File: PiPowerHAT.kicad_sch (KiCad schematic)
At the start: 34 parts, among them J8 2444

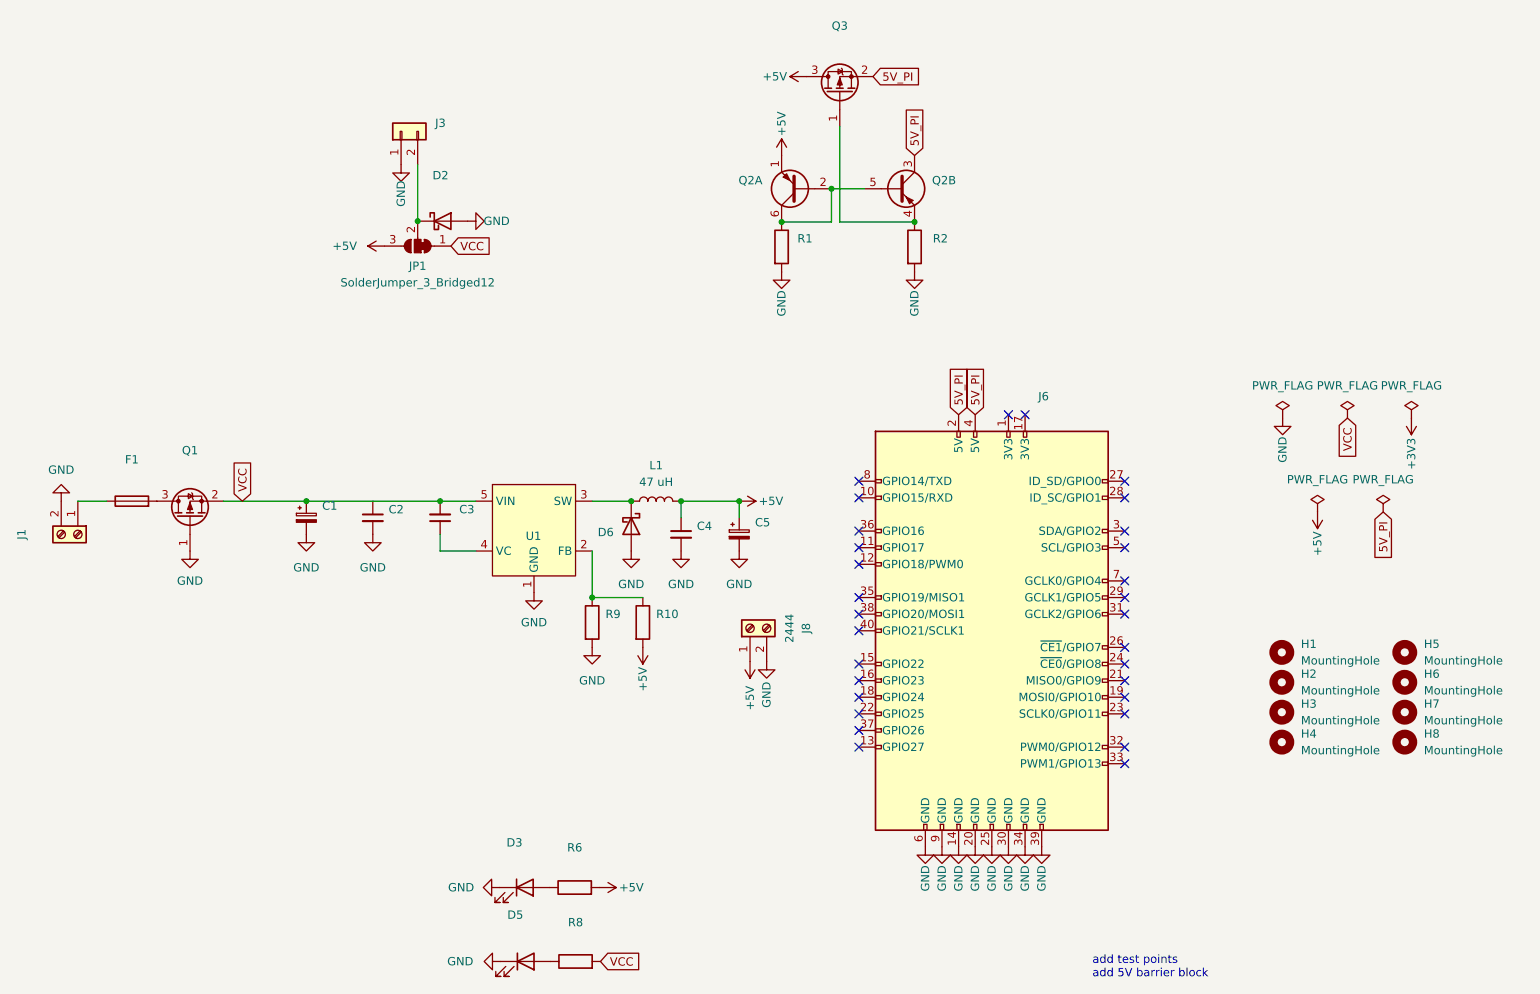
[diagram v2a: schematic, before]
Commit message: BOM Updates
Mounting holes and other items not sent to automated manufacture excluded from BOM
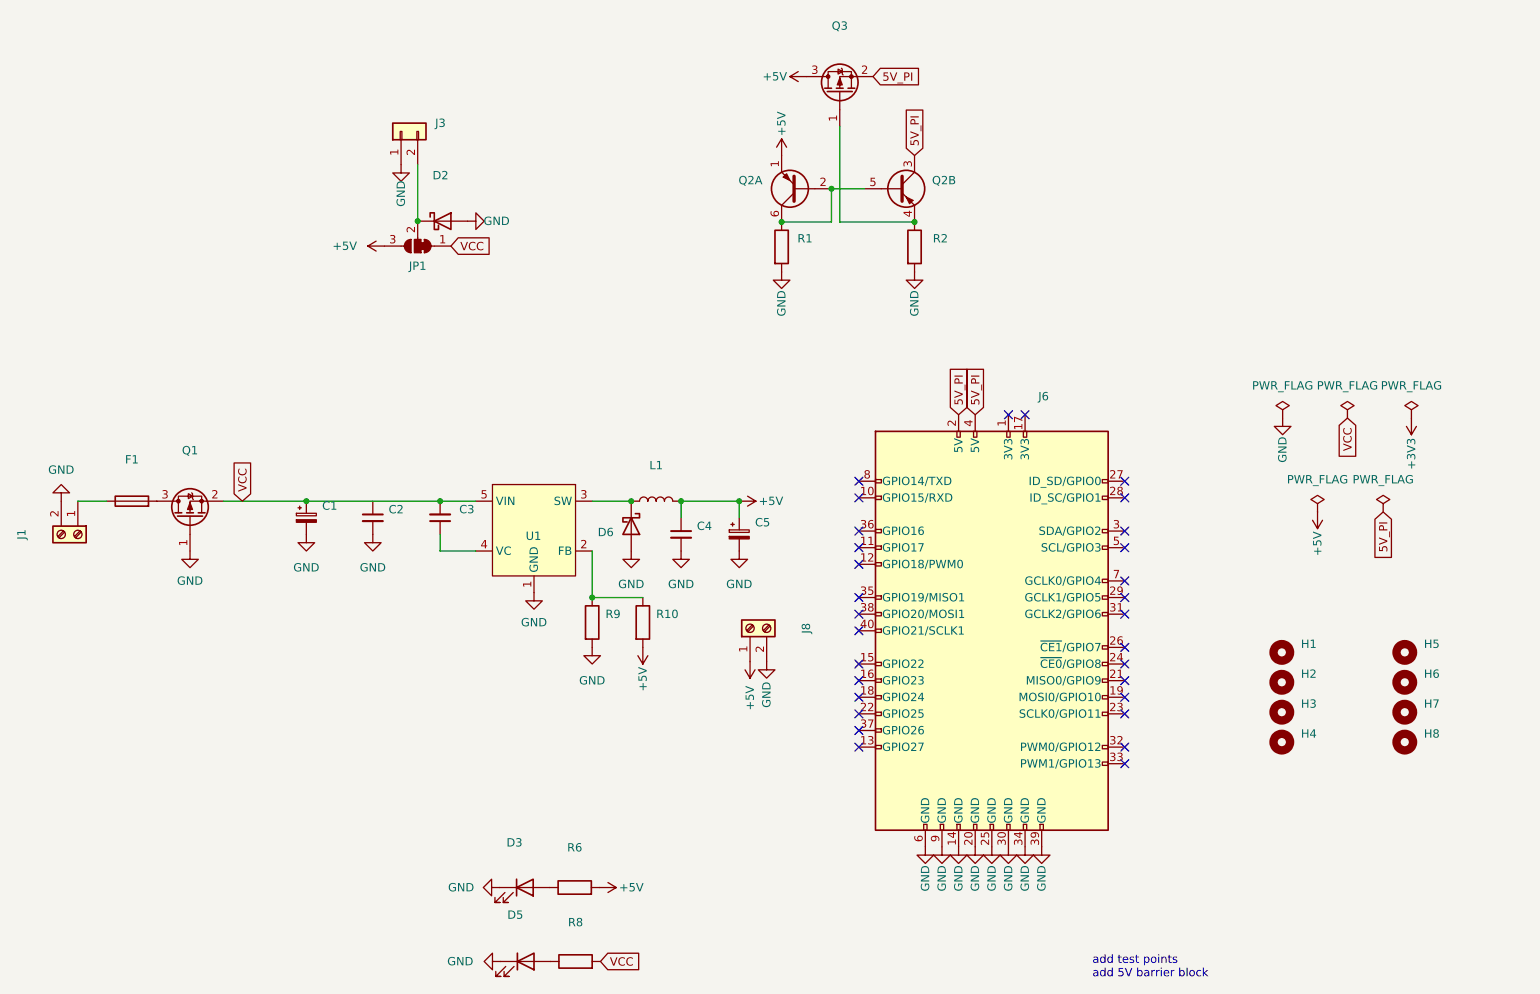
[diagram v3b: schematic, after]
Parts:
- H1, H2, H3, H4: value MountingHole -> (none); footprint MountingHole:MountingHole_2.7mm_M2.5_DIN965_Pad -> (none); now left out of the parts list
- H5, H6, H7, H8: value MountingHole -> (none); footprint MountingHole:MountingHole_3.5mm -> (none); now left out of the parts list
- J1, J3, J6: now left out of the parts list
- J8: value 2444 -> (none); footprint TerminalBlock_4Ucon:TerminalBlock_4Ucon_1x02_P3.50mm_Horizontal -> (none); now left out of the parts list
- JP1: value SolderJumper_3_Bridged12 -> (none); footprint Jumper:SolderJumper-3_P1.3mm_Bridged2Bar12_RoundedPad1.0x1.5mm -> (none); now left out of the parts list
- L1: value 47 uH -> (none); footprint Inductor_SMD:L_12x12mm_H6mm -> (none); JLC C497913 -> (none); LCSC (none) -> C497913
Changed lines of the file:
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@@
   )
   (symbol (lib_id "Mechanical:MountingHole") (at 206.629 132.461 0) (unit 1)
-    (in_bom yes) (on_board yes) (fields_autoplaced)
+    (in_bom no) (on_board yes) (fields_autoplaced)
     (property "Reference" "H4" (id 0) (at 209.55 131.1909 0)
       (effects (font (size 1.27 1.27)) (justify left))
     )
-    (property "Value" "MountingHole" (id 1) (at 209.55 133.7309 0)
-      (effects (font (size 1.27 1.27)) (justify left))
-    )
-    (property "Footprint" "MountingHole:MountingHole_2.7mm_M2.5_DIN965_Pad" (id 2) (at 206.629 132.461 0)
+    (property "Value" "" (id 1) (at 209.55 133.7309 0)
+      (effects (font (size 1.27 1.27)) (justify left))
+    )
+    (property "Footprint" "" (id 2) (at 206.629 132.461 0)
       (effects (font (size 1.27 1.27)) hide)
     )
@@
   )
   (symbol (lib_id "Connector_Generic:Conn_01x02") (at 72.009 39.116 90) (unit 1)
-    (in_bom yes) (on_board yes) (fields_autoplaced)
+    (in_bom no) (on_board yes) (fields_autoplaced)
     (property "Reference" "J3" (id 0) (at 77.216 37.8459 90)
       (effects (font (size 1.27 1.27)) (justify right))
@@
   )
   (symbol (lib_id "Connector:Screw_Terminal_01x02") (at 22.606 100.711 270) (unit 1)
-    (in_bom yes) (on_board yes)
+    (in_bom no) (on_board yes)
     (property "Reference" "J1" (id 0) (at 14.0208 100.711 0))
     (property "Value" "" (id 1) (at 16.5608 100.711 0))
@@
   )
   (symbol (lib_id "Mechanical:MountingHole") (at 206.629 127.889 0) (unit 1)
-    (in_bom yes) (on_board yes) (fields_autoplaced)
+    (in_bom no) (on_board yes) (fields_autoplaced)
     (property "Reference" "H3" (id 0) (at 209.55 126.6189 0)
       (effects (font (size 1.27 1.27)) (justify left))
     )
-    (property "Value" "MountingHole" (id 1) (at 209.55 129.1589 0)
-      (effects (font (size 1.27 1.27)) (justify left))
-    )
-    (property "Footprint" "MountingHole:MountingHole_2.7mm_M2.5_DIN965_Pad" (id 2) (at 206.629 127.889 0)
+    (property "Value" "" (id 1) (at 209.55 129.1589 0)
+      (effects (font (size 1.27 1.27)) (justify left))
+    )
+    (property "Footprint" "" (id 2) (at 206.629 127.889 0)
       (effects (font (size 1.27 1.27)) hide)
     )
@@
   )
   (symbol (lib_id "Mechanical:MountingHole") (at 206.629 123.317 0) (unit 1)
-    (in_bom yes) (on_board yes) (fields_autoplaced)
+    (in_bom no) (on_board yes) (fields_autoplaced)
     (property "Reference" "H2" (id 0) (at 209.55 122.0469 0)
       (effects (font (size 1.27 1.27)) (justify left))
     )
-    (property "Value" "MountingHole" (id 1) (at 209.55 124.5869 0)
-      (effects (font (size 1.27 1.27)) (justify left))
-    )
-    (property "Footprint" "MountingHole:MountingHole_2.7mm_M2.5_DIN965_Pad" (id 2) (at 206.629 123.317 0)
+    (property "Value" "" (id 1) (at 209.55 124.5869 0)
+      (effects (font (size 1.27 1.27)) (justify left))
+    )
+    (property "Footprint" "" (id 2) (at 206.629 123.317 0)
       (effects (font (size 1.27 1.27)) hide)
     )
@@
   )
   (symbol (lib_id "Mechanical:MountingHole") (at 225.425 127.889 0) (unit 1)
-    (in_bom yes) (on_board yes) (fields_autoplaced)
+    (in_bom no) (on_board yes) (fields_autoplaced)
     (property "Reference" "H7" (id 0) (at 228.346 126.6189 0)
       (effects (font (size 1.27 1.27)) (justify left))
     )
-    (property "Value" "MountingHole" (id 1) (at 228.346 129.1589 0)
-      (effects (font (size 1.27 1.27)) (justify left))
-    )
-    (property "Footprint" "MountingHole:MountingHole_3.5mm" (id 2) (at 225.425 127.889 0)
+    (property "Value" "" (id 1) (at 228.346 129.1589 0)
+      (effects (font (size 1.27 1.27)) (justify left))
+    )
+    (property "Footprint" "" (id 2) (at 225.425 127.889 0)
       (effects (font (size 1.27 1.27)) hide)
     )
@@
   )
   (symbol (lib_id "Mechanical:MountingHole") (at 225.425 118.745 0) (unit 1)
-    (in_bom yes) (on_board yes) (fields_autoplaced)
+    (in_bom no) (on_board yes) (fields_autoplaced)
     (property "Reference" "H5" (id 0) (at 228.346 117.4749 0)
       (effects (font (size 1.27 1.27)) (justify left))
     )
-    (property "Value" "MountingHole" (id 1) (at 228.346 120.0149 0)
-      (effects (font (size 1.27 1.27)) (justify left))
-    )
-    (property "Footprint" "MountingHole:MountingHole_3.5mm" (id 2) (at 225.425 118.745 0)
+    (property "Value" "" (id 1) (at 228.346 120.0149 0)
+      (effects (font (size 1.27 1.27)) (justify left))
+    )
+    (property "Footprint" "" (id 2) (at 225.425 118.745 0)
       (effects (font (size 1.27 1.27)) hide)
     )
@@
   )
   (symbol (lib_id "Jumper:SolderJumper_3_Bridged12") (at 74.549 56.642 180) (unit 1)
-    (in_bom yes) (on_board yes) (fields_autoplaced)
+    (in_bom no) (on_board yes) (fields_autoplaced)
     (property "Reference" "JP1" (id 0) (at 74.549 59.69 0))
-    (property "Value" "SolderJumper_3_Bridged12" (id 1) (at 74.549 62.23 0))
-    (property "Footprint" "Jumper:SolderJumper-3_P1.3mm_Bridged2Bar12_RoundedPad1.0x1.5mm" (id 2) (at 74.549 56.642 0)
+    (property "Value" "" (id 1) (at 74.549 62.23 0))
+    (property "Footprint" "" (id 2) (at 74.549 56.642 0)
       (effects (font (size 1.27 1.27)) hide)
     )
@@
   )
   (symbol (lib_id "Mechanical:MountingHole") (at 225.425 132.461 0) (unit 1)
-    (in_bom yes) (on_board yes) (fields_autoplaced)
+    (in_bom no) (on_board yes) (fields_autoplaced)
     (property "Reference" "H8" (id 0) (at 228.346 131.1909 0)
       (effects (font (size 1.27 1.27)) (justify left))
     )
-    (property "Value" "MountingHole" (id 1) (at 228.346 133.7309 0)
-      (effects (font (size 1.27 1.27)) (justify left))
-    )
-    (property "Footprint" "MountingHole:MountingHole_3.5mm" (id 2) (at 225.425 132.461 0)
+    (property "Value" "" (id 1) (at 228.346 133.7309 0)
+      (effects (font (size 1.27 1.27)) (justify left))
+    )
+    (property "Footprint" "" (id 2) (at 225.425 132.461 0)
       (effects (font (size 1.27 1.27)) hide)
     )
@@
   )
   (symbol (lib_id "Connector:Screw_Terminal_01x02") (at 125.349 115.062 90) (unit 1)
-    (in_bom yes) (on_board yes)
+    (in_bom no) (on_board yes)
     (property "Reference" "J8" (id 0) (at 133.9342 115.062 0))
-    (property "Value" "2444" (id 1) (at 131.3942 115.062 0))
-    (property "Footprint" "TerminalBlock_4Ucon:TerminalBlock_4Ucon_1x02_P3.50mm_Horizontal" (id 2) (at 125.349 115.062 0)
+    (property "Value" "" (id 1) (at 131.3942 115.062 0))
+    (property "Footprint" "" (id 2) (at 125.349 115.062 0)
       (effects (font (size 1.27 1.27)) hide)
     )
@@
   )
   (symbol (lib_id "Mechanical:MountingHole") (at 225.425 123.317 0) (unit 1)
-    (in_bom yes) (on_board yes) (fields_autoplaced)
+    (in_bom no) (on_board yes) (fields_autoplaced)
     (property "Reference" "H6" (id 0) (at 228.346 122.0469 0)
       (effects (font (size 1.27 1.27)) (justify left))
     )
-    (property "Value" "MountingHole" (id 1) (at 228.346 124.5869 0)
-      (effects (font (size 1.27 1.27)) (justify left))
-    )
-    (property "Footprint" "MountingHole:MountingHole_3.5mm" (id 2) (at 225.425 123.317 0)
+    (property "Value" "" (id 1) (at 228.346 124.5869 0)
+      (effects (font (size 1.27 1.27)) (justify left))
+    )
+    (property "Footprint" "" (id 2) (at 225.425 123.317 0)
       (effects (font (size 1.27 1.27)) hide)
     )
@@
     (in_bom yes) (on_board yes) (fields_autoplaced)
     (property "Reference" "L1" (id 0) (at 110.998 90.17 90))
-    (property "Value" "47 uH" (id 1) (at 110.998 92.71 90))
-    (property "Footprint" "Inductor_SMD:L_12x12mm_H6mm" (id 2) (at 110.998 95.631 0)
+    (property "Value" "" (id 1) (at 110.998 92.71 90))
+    (property "Footprint" "" (id 2) (at 110.998 95.631 0)
       (effects (font (size 1.27 1.27)) hide)
     )
@@
       (effects (font (size 1.27 1.27)) hide)
     )
-    (property "JLC" "C497913" (id 4) (at 110.998 95.631 90)
+    (property "LCSC" "C497913" (id 4) (at 110.998 95.631 90)
       (effects (font (size 1.27 1.27)) hide)
     )
@@
   )
   (symbol (lib_id "Connector:Raspberry_Pi_2_3") (at 162.306 115.443 0) (unit 1)
-    (in_bom yes) (on_board yes)
+    (in_bom no) (on_board yes)
     (property "Reference" "J6" (id 0) (at 169.4054 79.629 0)
       (effects (font (size 1.27 1.27)) (justify left))
@@
   )
   (symbol (lib_id "Mechanical:MountingHole") (at 206.629 118.745 0) (unit 1)
-    (in_bom yes) (on_board yes) (fields_autoplaced)
+    (in_bom no) (on_board yes) (fields_autoplaced)
     (property "Reference" "H1" (id 0) (at 209.55 117.4749 0)
       (effects (font (size 1.27 1.27)) (justify left))
     )
-    (property "Value" "MountingHole" (id 1) (at 209.55 120.0149 0)
-      (effects (font (size 1.27 1.27)) (justify left))
-    )
-    (property "Footprint" "MountingHole:MountingHole_2.7mm_M2.5_DIN965_Pad" (id 2) (at 206.629 118.745 0)
+    (property "Value" "" (id 1) (at 209.55 120.0149 0)
+      (effects (font (size 1.27 1.27)) (justify left))
+    )
+    (property "Footprint" "" (id 2) (at 206.629 118.745 0)
       (effects (font (size 1.27 1.27)) hide)
     )
@@
     )
     (path "/bcd6e405-0bb1-44eb-adb9-068c36c8144d"
-      (reference "J8") (unit 1) (value "2444") (footprint "TerminalBlock_4Ucon:TerminalBlock_4Ucon_1x02_P3.50mm_Horizontal")
+      (reference "J8") (unit 1) (value "2444") (footprint "Connector_JST:JST_XH_B2B-XH-A_1x02_P2.50mm_Vertical")
     )
     (path "/9d09f6cd-97f0-4b1c-bd0b-800cff10151a"
